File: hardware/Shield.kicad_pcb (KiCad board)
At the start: 2 copper layers, 70.1 x 40.6 mm, 29 parts, among them IC1 TP4056-42-ESOP8, P1 CONN_14_1, P2 CONN_14_2, SW1 JS202011SCQN

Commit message: changed diode ref because missing in fab catalog
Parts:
- D1, D2, D3, D4, D5, D6: value PMEG6010CEH,115 -> 1N5819W
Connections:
- P1 pad 5: (no net) -> Net-(P1-Pad5)
- P1 pad A0: (no net) -> Net-(P1-PadA0)
- P1 pad A5: (no net) -> Net-(P1-PadA5)
- P1 pad A6: (no net) -> Net-(P1-PadA6)
- P1 pad AREF: (no net) -> Net-(P1-PadAREF)
- P2 pad 10: (no net) -> Net-(P2-Pad10)
- P2 pad 11: (no net) -> Net-(P2-Pad11)
- P2 pad 12: (no net) -> Net-(P2-Pad12)
- P2 pad 13: (no net) -> Net-(P2-Pad13)
- P2 pad 14: (no net) -> Net-(P2-Pad14)
- P2 pad 5V: (no net) -> Net-(P2-Pad5V)
- P2 pad 6: (no net) -> Net-(P2-Pad6)
- P2 pad 7: (no net) -> Net-(P2-Pad7)
- P2 pad 8: (no net) -> Net-(P2-Pad8)
- P2 pad 9: (no net) -> Net-(P2-Pad9)
- P2 pad RESET: (no net) -> Net-(P2-PadRESET)
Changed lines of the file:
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@@
     (zones 0)
     (modules 29)
-    (nets 24)
+    (nets 40)
   )
   (page A4)
   (title_block
     (title "MkrFox1200 Wind Shield")
-    (date 2021-12-03)
+    (date 2021-12-07)
     (rev 1.0)
     (company OpenWindMap)
@@
   (layers
     (0 F.Cu signal)
-    (31 B.Cu signal)
+    (31 B.Cu signal hide)
     (32 B.Adhes user)
     (33 F.Adhes user)
@@
       (drillshape 0)
       (scaleselection 1)
-      (outputdirectory "Gerber/"))
+      (outputdirectory ""))
   )
   (net 0 "")
@@
   (net 22 VIN)
   (net 23 MGND)
+  (net 24 "Net-(P1-Pad5)")
+  (net 25 "Net-(P1-PadA6)")
+  (net 26 "Net-(P1-PadA5)")
+  (net 27 "Net-(P1-PadA0)")
+  (net 28 "Net-(P1-PadAREF)")
+  (net 29 "Net-(P2-Pad6)")
+  (net 30 "Net-(P2-Pad7)")
+  (net 31 "Net-(P2-Pad8)")
+  (net 32 "Net-(P2-Pad9)")
+  (net 33 "Net-(P2-Pad10)")
+  (net 34 "Net-(P2-Pad11)")
+  (net 35 "Net-(P2-Pad12)")
+  (net 36 "Net-(P2-Pad13)")
+  (net 37 "Net-(P2-Pad14)")
+  (net 38 "Net-(P2-PadRESET)")
+  (net 39 "Net-(P2-Pad5V)")
   (net_class Default "Ceci est la Netclass par défaut."
     (clearance 0.2)
@@
     (add_net "Net-(J_SENSOR1-Pad1)")
     (add_net "Net-(J_SENSOR1-Pad6)")
+    (add_net "Net-(P1-Pad5)")
+    (add_net "Net-(P1-PadA0)")
+    (add_net "Net-(P1-PadA5)")
+    (add_net "Net-(P1-PadA6)")
+    (add_net "Net-(P1-PadAREF)")
+    (add_net "Net-(P2-Pad10)")
+    (add_net "Net-(P2-Pad11)")
+    (add_net "Net-(P2-Pad12)")
+    (add_net "Net-(P2-Pad13)")
+    (add_net "Net-(P2-Pad14)")
+    (add_net "Net-(P2-Pad5V)")
+    (add_net "Net-(P2-Pad6)")
+    (add_net "Net-(P2-Pad7)")
+    (add_net "Net-(P2-Pad8)")
+    (add_net "Net-(P2-Pad9)")
+    (add_net "Net-(P2-PadRESET)")
     (add_net "Net-(SW1-Pad3)")
     (add_net "Net-(SW1-Pad4)")
@@
     (fp_line (start -17.78 -1.27) (end 17.78 -1.27) (layer F.SilkS) (width 0.12))
     (fp_line (start -17.78 -3.81) (end -17.78 -1.27) (layer F.SilkS) (width 0.12))
-    (pad 6 thru_hole circle (at 16.51 -2.54 180) (size 1.524 1.524) (drill 0.762) (layers *.Cu *.Mask))
-    (pad 7 thru_hole circle (at 13.97 -2.54 180) (size 1.524 1.524) (drill 0.762) (layers *.Cu *.Mask))
-    (pad 8 thru_hole circle (at 11.43 -2.54 180) (size 1.524 1.524) (drill 0.762) (layers *.Cu *.Mask))
-    (pad 9 thru_hole circle (at 8.89 -2.54 180) (size 1.524 1.524) (drill 0.762) (layers *.Cu *.Mask))
-    (pad 10 thru_hole circle (at 6.35 -2.54 180) (size 1.524 1.524) (drill 0.762) (layers *.Cu *.Mask))
-    (pad 11 thru_hole circle (at 3.81 -2.54 180) (size 1.524 1.524) (drill 0.762) (layers *.Cu *.Mask))
-    (pad 12 thru_hole circle (at 1.27 -2.54 180) (size 1.524 1.524) (drill 0.762) (layers *.Cu *.Mask))
-    (pad 13 thru_hole circle (at -1.27 -2.54 180) (size 1.524 1.524) (drill 0.762) (layers *.Cu *.Mask))
-    (pad 14 thru_hole circle (at -3.81 -2.54 180) (size 1.524 1.524) (drill 0.762) (layers *.Cu *.Mask))
-    (pad RESET thru_hole circle (at -6.35 -2.54 180) (size 1.524 1.524) (drill 0.762) (layers *.Cu *.Mask))
+    (pad 6 thru_hole circle (at 16.51 -2.54 180) (size 1.524 1.524) (drill 0.762) (layers *.Cu *.Mask)
+      (net 29 "Net-(P2-Pad6)"))
+    (pad 7 thru_hole circle (at 13.97 -2.54 180) (size 1.524 1.524) (drill 0.762) (layers *.Cu *.Mask)
+      (net 30 "Net-(P2-Pad7)"))
+    (pad 8 thru_hole circle (at 11.43 -2.54 180) (size 1.524 1.524) (drill 0.762) (layers *.Cu *.Mask)
+      (net 31 "Net-(P2-Pad8)"))
+    (pad 9 thru_hole circle (at 8.89 -2.54 180) (size 1.524 1.524) (drill 0.762) (layers *.Cu *.Mask)
+      (net 32 "Net-(P2-Pad9)"))
+    (pad 10 thru_hole circle (at 6.35 -2.54 180) (size 1.524 1.524) (drill 0.762) (layers *.Cu *.Mask)
+      (net 33 "Net-(P2-Pad10)"))
+    (pad 11 thru_hole circle (at 3.81 -2.54 180) (size 1.524 1.524) (drill 0.762) (layers *.Cu *.Mask)
+      (net 34 "Net-(P2-Pad11)"))
+    (pad 12 thru_hole circle (at 1.27 -2.54 180) (size 1.524 1.524) (drill 0.762) (layers *.Cu *.Mask)
+      (net 35 "Net-(P2-Pad12)"))
+    (pad 13 thru_hole circle (at -1.27 -2.54 180) (size 1.524 1.524) (drill 0.762) (layers *.Cu *.Mask)
+      (net 36 "Net-(P2-Pad13)"))
+    (pad 14 thru_hole circle (at -3.81 -2.54 180) (size 1.524 1.524) (drill 0.762) (layers *.Cu *.Mask)
+      (net 37 "Net-(P2-Pad14)"))
+    (pad RESET thru_hole circle (at -6.35 -2.54 180) (size 1.524 1.524) (drill 0.762) (layers *.Cu *.Mask)
+      (net 38 "Net-(P2-PadRESET)"))
     (pad GND thru_hole circle (at -8.89 -2.54 180) (size 1.524 1.524) (drill 0.762) (layers *.Cu *.Mask)
       (net 23 MGND))
@@
     (pad VIN thru_hole circle (at -13.97 -2.54 180) (size 1.524 1.524) (drill 0.762) (layers *.Cu *.Mask)
       (net 22 VIN))
-    (pad 5V thru_hole circle (at -16.51 -2.54 180) (size 1.524 1.524) (drill 0.762) (layers *.Cu *.Mask))
+    (pad 5V thru_hole circle (at -16.51 -2.54 180) (size 1.524 1.524) (drill 0.762) (layers *.Cu *.Mask)
+      (net 39 "Net-(P2-Pad5V)"))
   )
   (module JLCPCB_FP:CONN14_FP1 (layer F.Cu)
@@
     (fp_line (start -17.78 -1.27) (end 17.78 -1.27) (layer F.SilkS) (width 0.12))
     (fp_line (start -17.78 -3.81) (end -17.78 -1.27) (layer F.SilkS) (width 0.12))
-    (pad 5 thru_hole circle (at 16.51 -2.54 180) (size 1.524 1.524) (drill 0.762) (layers *.Cu *.Mask))
+    (pad 5 thru_hole circle (at 16.51 -2.54 180) (size 1.524 1.524) (drill 0.762) (layers *.Cu *.Mask)
+      (net 24 "Net-(P1-Pad5)"))
     (pad 4 thru_hole circle (at 13.97 -2.54 180) (size 1.524 1.524) (drill 0.762) (layers *.Cu *.Mask)
       (net 19 D4))
@@
     (pad 0 thru_hole circle (at 3.81 -2.54 180) (size 1.524 1.524) (drill 0.762) (layers *.Cu *.Mask)
       (net 9 D0))
-    (pad A6 thru_hole circle (at 1.27 -2.54 180) (size 1.524 1.524) (drill 0.762) (layers *.Cu *.Mask))
-    (pad A5 thru_hole circle (at -1.27 -2.54 180) (size 1.524 1.524) (drill 0.762) (layers *.Cu *.Mask))
+    (pad A6 thru_hole circle (at 1.27 -2.54 180) (size 1.524 1.524) (drill 0.762) (layers *.Cu *.Mask)
+      (net 25 "Net-(P1-PadA6)"))
+    (pad A5 thru_hole circle (at -1.27 -2.54 180) (size 1.524 1.524) (drill 0.762) (layers *.Cu *.Mask)
+      (net 26 "Net-(P1-PadA5)"))
     (pad A4 thru_hole circle (at -3.81 -2.54 180) (size 1.524 1.524) (drill 0.762) (layers *.Cu *.Mask)
       (net 18 A4))
@@
     (pad A1 thru_hole circle (at -11.43 -2.54 180) (size 1.524 1.524) (drill 0.762) (layers *.Cu *.Mask)
       (net 10 D1A1))
-    (pad A0 thru_hole circle (at -13.97 -2.54 180) (size 1.524 1.524) (drill 0.762) (layers *.Cu *.Mask))
-    (pad AREF thru_hole circle (at -16.51 -2.54 180) (size 1.524 1.524) (drill 0.762) (layers *.Cu *.Mask))
+    (pad A0 thru_hole circle (at -13.97 -2.54 180) (size 1.524 1.524) (drill 0.762) (layers *.Cu *.Mask)
+      (net 27 "Net-(P1-PadA0)"))
+    (pad AREF thru_hole circle (at -16.51 -2.54 180) (size 1.524 1.524) (drill 0.762) (layers *.Cu *.Mask)
+      (net 28 "Net-(P1-PadAREF)"))
   )
   (module JLCPCB_FP:DS1133S60APS (layer F.Cu)
@@
       (effects (font (size 1.27 1.27) (thickness 0.254)))
     )
-    (fp_text value PMEG6010CEH,115 (at 0 0 90) (layer F.SilkS) hide
+    (fp_text value 1N5819W (at 0 0 90) (layer F.SilkS) hide
       (effects (font (size 1.27 1.27) (thickness 0.254)))
     )
@@
       (effects (font (size 1.27 1.27) (thickness 0.254)))
     )
-    (fp_text value PMEG6010CEH,115 (at 0 0 90) (layer F.SilkS) hide
+    (fp_text value 1N5819W (at 0 0 90) (layer F.SilkS) hide
       (effects (font (size 1.27 1.27) (thickness 0.254)))
     )
@@
       (effects (font (size 1.27 1.27) (thickness 0.254)))
     )
-    (fp_text value PMEG6010CEH,115 (at 0 0 90) (layer F.SilkS) hide
+    (fp_text value 1N5819W (at 0 0 90) (layer F.SilkS) hide
       (effects (font (size 1.27 1.27) (thickness 0.254)))
     )
@@
       (effects (font (size 1.27 1.27) (thickness 0.254)))
     )
-    (fp_text value PMEG6010CEH,115 (at 0 0 90) (layer F.SilkS) hide
+    (fp_text value 1N5819W (at 0 0 90) (layer F.SilkS) hide
       (effects (font (size 1.27 1.27) (thickness 0.254)))
     )
@@
       (effects (font (size 1.27 1.27) (thickness 0.254)))
     )
-    (fp_text value PMEG6010CEH,115 (at 0 0 90) (layer F.SilkS) hide
+    (fp_text value 1N5819W (at 0 0 90) (layer F.SilkS) hide
       (effects (font (size 1.27 1.27) (thickness 0.254)))
     )
@@
       (effects (font (size 1.27 1.27) (thickness 0.254)))
     )
-    (fp_text value PMEG6010CEH,115 (at 0 0 90) (layer F.SilkS) hide
-      (effects (font (size 1.27 1.27) (thickness 0.254)))
-    )
+    (fp_text value 1N5819W (at 0 0 90) (layer F.SilkS) hide
+      (effects (font (size 1.27 1.27) (thickness 0.254)))
+    )

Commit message: reorg sockets
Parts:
- moved J_SENSOR1 57.5 mm to (62.0, 83.5), turned to 90 degrees
- moved J_PV1 10.3 mm to (117.2, 98.1)
- moved J_BAT1 9.05 mm to (133.2, 98.9)
- moved JS1 4.42 mm to (93.6, 97.3)
- moved JS2 4.42 mm to (103.7, 97.3)
- moved C1 0.50 mm to (105.7, 74.5)
- moved R1 0.41 mm to (100.0, 74.1)
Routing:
- net Wire4: track 40.7 -> 72.9 mm, vias 3 -> 5
- net VPV: track 34.6 -> 53.6 mm
- net Wire1: track 88.6 -> 70.7 mm, vias 4 -> 5
- net GND: track 116.0 -> 100.1 mm
- net Wire3: track 55.2 -> 69.8 mm, vias 3 -> 5
- net VBAT: track 95.5 -> 86.7 mm
- net MGND: track 135.7 -> 135.9 mm, vias 3 -> 1
- removed copper zone on B.Cu, net GND
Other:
- board size 70.1 x 40.6 mm -> 80.8 x 39.7 mm
- board text added: "MkrfoxWindShield v1.1"
- board text added: "On / Off"
- board text added: "Solar Pwr IN"
- board text removed: "MkrfoxWindShield v1.0"
- board text removed: "On/ Off"
- board text removed: "Pwr IN"

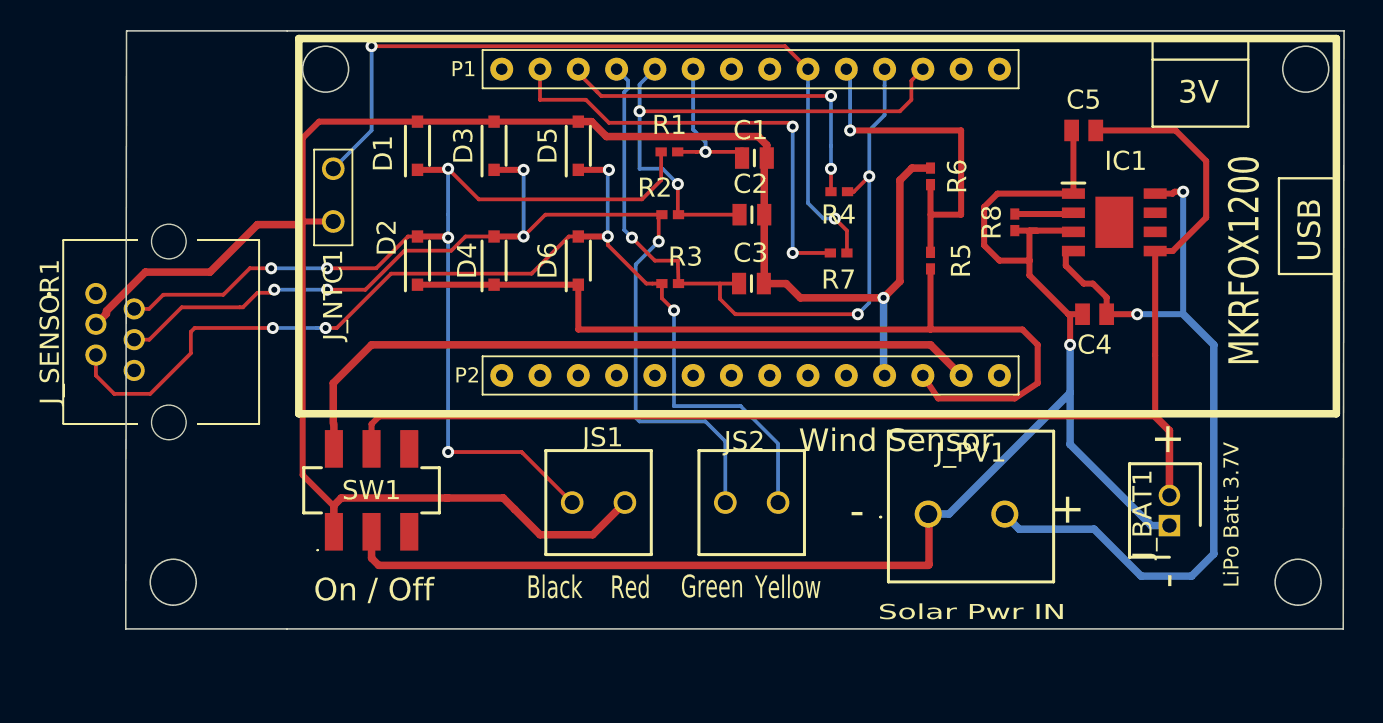
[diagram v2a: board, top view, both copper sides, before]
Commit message: modified hardware: position of sockets, points for external switch
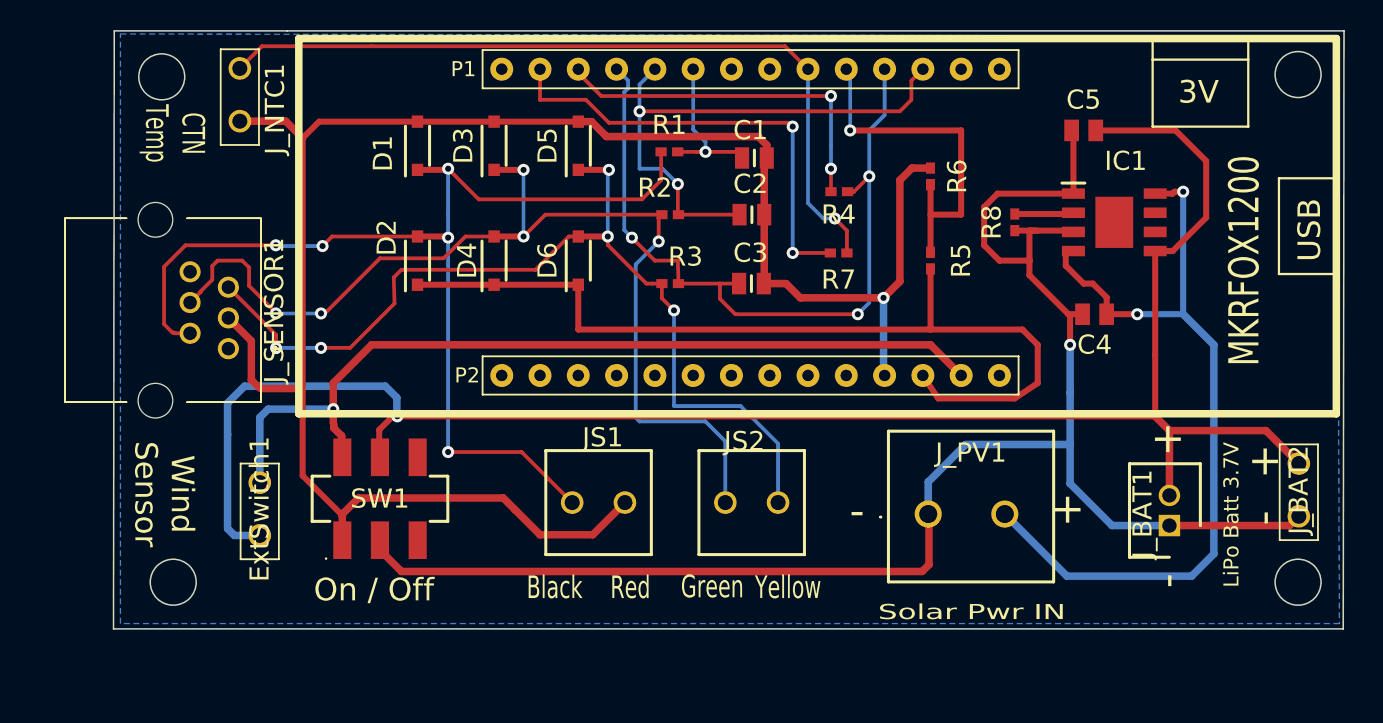
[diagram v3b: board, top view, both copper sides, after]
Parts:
- added ExtSwitch1: KF350-3.5-2P, JLCPCB_FP:SolderPoints, F.Cu at (72.8, 96.0)
- added J_BAT2: KF350-3.5-2P, JLCPCB_FP:SolderPoints, F.Cu at (141.8, 94.7)
- moved J_SENSOR1 9.52 mm to (70.8, 87.1), turned to 270 degrees
- moved J_NTC1 9.09 mm to (71.5, 68.5)
- moved SW1 0.79 mm to (80.8, 97.1)
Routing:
- net VBAT: track 86.7 -> 119.9 mm, vias 0 -> 1
- net VIN: track 47.9 -> 58.1 mm, vias 0 -> 1
- net Wire4: track 72.9 -> 63.4 mm
- net GND: track 100.1 -> 109.5 mm
- net MGND: track 135.9 -> 127.1 mm
- net Wire1: track 70.7 -> 73.4 mm
- net Wire3: track 69.8 -> 69.1 mm
- net A4: track 52.5 -> 52.6 mm, vias 2 -> 1
- added copper zone on B.Cu, net MGND
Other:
- board size 80.8 x 39.7 mm -> 81.6 x 39.7 mm
- board text added: "CTN Temp"
